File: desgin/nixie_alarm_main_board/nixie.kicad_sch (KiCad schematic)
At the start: 31 parts, among them IC2 HV5530PG-G, IC4 HV5530PG-G, IC6 CD40109BQNSRQ1, Q2 DMN60H080DS-13, Q3 DMN60H080DS-13, Q4 DMN60H080DS-13, Q5 DMN60H080DS-13, Q6 DMN60H080DS-13, Q7 DMN60H080DS-13

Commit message: filter caps
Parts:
- added C6, C7, C8, C9: 100nF 25V, GRM033D70J224ME01D, symbol SamacSys_Parts:GRM033R71E101KA01J
- added R36, R37, R38, R39, R40, R41: 51kΩ, RESC2012X60N, symbol SamacSys_Parts:RK73H2ATTE1003F
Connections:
- net +12V: now also C7.1, C8.1, C9.1
- net GND: now also C6.2, C7.2, C8.2, C9.2, R36.1, R37.1, R38.1, R39.1, R40.1, R41.1; no longer Q2.2 (S), Q3.2 (S), Q4.2 (S), Q5.2 (S), Q6.2 (S), Q7.2 (S)
- net +5V renamed +3.3V
- net +3.3V: now also C6.1
- new net: Q6.2 (S), R40.2
- new net: Q4.2 (S), R38.2
- new net: Q5.2 (S), R39.2
- new net: Q7.2 (S), R41.2
- new net: Q3.2 (S), R37.2
- new net: Q2.2 (S), R36.2
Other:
- moved on the sheet: IC6

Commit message: new rezistors
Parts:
- C6, C7, C8, C9: footprint GRM033D70J224ME01D -> Capacitor_SMD:C_0805_2012Metric_Pad1.18x1.45mm_HandSolder
- R21, R27: value 402kΩ 1/4W -> 390kΩ 1/2W; footprint RESC2012X60N -> Resistor_SMD:R_0805_2012Metric_Pad1.20x1.40mm_HandSolder
- R22, R23, R25, R28, R31, R33: value 25kΩ -> 27kΩ; footprint RESC2012X60N -> Resistor_SMD:R_0805_2012Metric_Pad1.20x1.40mm_HandSolder
- R36, R37, R38, R39, R40, R41: footprint RESC2012X60N -> Resistor_SMD:R_0805_2012Metric_Pad1.20x1.40mm_HandSolder
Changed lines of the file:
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@@
 			)
 		)
-		(property "Footprint" "GRM033D70J224ME01D"
+		(property "Footprint" "Capacitor_SMD:C_0805_2012Metric_Pad1.18x1.45mm_HandSolder"
 			(at -66.218 115.824 0)
 			(effects
@@
 			)
 		)
-		(property "Footprint" "RESC2012X60N"
+		(property "Footprint" "Resistor_SMD:R_0805_2012Metric_Pad1.20x1.40mm_HandSolder"
 			(at 137.49 40.894 0)
 			(effects
@@
 			)
 		)
-		(property "Value" "25kΩ"
+		(property "Value" "27kΩ"
 			(at 254.508 54.864 90)
 			(effects
@@
 			)
 		)
-		(property "Footprint" "RESC2012X60N"
+		(property "Footprint" "Resistor_SMD:R_0805_2012Metric_Pad1.20x1.40mm_HandSolder"
 			(at 165.938 58.674 0)
 			(effects
@@
 			)
 		)
-		(property "Value" "25kΩ"
+		(property "Value" "27kΩ"
 			(at 67.564 53.848 90)
 			(effects
@@
 			)
 		)
-		(property "Footprint" "RESC2012X60N"
+		(property "Footprint" "Resistor_SMD:R_0805_2012Metric_Pad1.20x1.40mm_HandSolder"
 			(at -21.006 57.658 0)
 			(effects
@@
 			)
 		)
-		(property "Footprint" "RESC2012X60N"
+		(property "Footprint" "Resistor_SMD:R_0805_2012Metric_Pad1.20x1.40mm_HandSolder"
 			(at 176.098 40.64 0)
 			(effects
@@
 			)
 		)
-		(property "Footprint" "GRM033D70J224ME01D"
+		(property "Footprint" "Capacitor_SMD:C_0805_2012Metric_Pad1.18x1.45mm_HandSolder"
 			(at -28.372 115.824 0)
 			(effects
@@
 			)
 		)
-		(property "Value" "402kΩ 1/4W"
+		(property "Value" "390kΩ 1/2W"
 			(at 103.378 55.1179 90)
 			(effects
@@
 			)
 		)
-		(property "Footprint" "RESC2012X60N"
+		(property "Footprint" "Resistor_SMD:R_0805_2012Metric_Pad1.20x1.40mm_HandSolder"
 			(at 4.902 58.928 0)
 			(effects
@@
 			)
 		)
-		(property "Footprint" "RESC2012X60N"
+		(property "Footprint" "Resistor_SMD:R_0805_2012Metric_Pad1.20x1.40mm_HandSolder"
 			(at -10.846 39.624 0)
 			(effects
@@
 			)
 		)
-		(property "Value" "25kΩ"
+		(property "Value" "27kΩ"
 			(at 122.174 54.61 90)
 			(effects
@@
 			)
 		)
-		(property "Footprint" "RESC2012X60N"
+		(property "Footprint" "Resistor_SMD:R_0805_2012Metric_Pad1.20x1.40mm_HandSolder"
 			(at 33.35 58.674 0)
 			(effects
@@
 			)
 		)
-		(property "Footprint" "RESC2012X60N"
+		(property "Footprint" "Resistor_SMD:R_0805_2012Metric_Pad1.20x1.40mm_HandSolder"
 			(at 43.51 40.64 0)
 			(effects
@@
 			)
 		)
-		(property "Footprint" "GRM033D70J224ME01D"
+		(property "Footprint" "Capacitor_SMD:C_0805_2012Metric_Pad1.18x1.45mm_HandSolder"
 			(at -65.71 141.732 0)
 			(effects
@@
 			)
 		)
-		(property "Footprint" "RESC2012X60N"
+		(property "Footprint" "Resistor_SMD:R_0805_2012Metric_Pad1.20x1.40mm_HandSolder"
 			(at -50.216 40.132 0)
 			(effects
@@
 			)
 		)
-		(property "Footprint" "RESC2012X60N"
+		(property "Footprint" "Resistor_SMD:R_0805_2012Metric_Pad1.20x1.40mm_HandSolder"
 			(at 82.372 40.132 0)
 			(effects
@@
 			)
 		)
-		(property "Value" "25kΩ"
+		(property "Value" "27kΩ"
 			(at 161.036 55.118 90)
 			(effects
@@
 			)
 		)
-		(property "Footprint" "RESC2012X60N"
+		(property "Footprint" "Resistor_SMD:R_0805_2012Metric_Pad1.20x1.40mm_HandSolder"
 			(at 72.212 58.42 0)
 			(effects
@@
 			)
 		)
-		(property "Value" "25kΩ"
+		(property "Value" "27kΩ"
 			(at 215.9 55.118 90)
 			(effects
@@
 			)
 		)
-		(property "Footprint" "RESC2012X60N"
+		(property "Footprint" "Resistor_SMD:R_0805_2012Metric_Pad1.20x1.40mm_HandSolder"
 			(at 127.33 58.928 0)
 			(effects
@@
 			)
 		)
-		(property "Value" "402kΩ 1/4W"
+		(property "Value" "390kΩ 1/2W"
 			(at 196.342 54.1019 90)
 			(effects
@@
 			)
 		)
-		(property "Footprint" "RESC2012X60N"
+		(property "Footprint" "Resistor_SMD:R_0805_2012Metric_Pad1.20x1.40mm_HandSolder"
 			(at 97.866 57.912 0)
 			(effects
@@
 			)
 		)
-		(property "Footprint" "GRM033D70J224ME01D"
+		(property "Footprint" "Capacitor_SMD:C_0805_2012Metric_Pad1.18x1.45mm_HandSolder"
 			(at -27.864 141.732 0)
 			(effects
@@
 			)
 		)
-		(property "Value" "25kΩ"
+		(property "Value" "27kΩ"
 			(at 28.448 54.356 90)
 			(effects
@@
 			)
 		)
-		(property "Footprint" "RESC2012X60N"
+		(property "Footprint" "Resistor_SMD:R_0805_2012Metric_Pad1.20x1.40mm_HandSolder"
 			(at -60.376 58.166 0)
 			(effects

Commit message: new caps footprint
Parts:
- R24, R26, R29, R30, R32, R34: footprint ERJUP6 -> Resistor_SMD:R_0805_2012Metric_Pad1.20x1.40mm_HandSolder
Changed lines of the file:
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@@
 			)
 		)
-		(property "Footprint" "ERJUP6"
+		(property "Footprint" "Resistor_SMD:R_0805_2012Metric_Pad1.20x1.40mm_HandSolder"
 			(at 282.372 35.052 0)
 			(effects
@@
 			)
 		)
-		(property "Footprint" "ERJUP6"
+		(property "Footprint" "Resistor_SMD:R_0805_2012Metric_Pad1.20x1.40mm_HandSolder"
 			(at 189.154 34.544 0)
 			(effects
@@
 			)
 		)
-		(property "Footprint" "ERJUP6"
+		(property "Footprint" "Resistor_SMD:R_0805_2012Metric_Pad1.20x1.40mm_HandSolder"
 			(at 149.784 35.052 0)
 			(effects
@@
 			)
 		)
-		(property "Footprint" "ERJUP6"
+		(property "Footprint" "Resistor_SMD:R_0805_2012Metric_Pad1.20x1.40mm_HandSolder"
 			(at 243.51 35.56 0)
 			(effects
@@
 			)
 		)
-		(property "Footprint" "ERJUP6"
+		(property "Footprint" "Resistor_SMD:R_0805_2012Metric_Pad1.20x1.40mm_HandSolder"
 			(at 337.49 35.814 0)
 			(effects
@@
 			)
 		)
-		(property "Footprint" "ERJUP6"
+		(property "Footprint" "Resistor_SMD:R_0805_2012Metric_Pad1.20x1.40mm_HandSolder"
 			(at 376.098 35.56 0)
 			(effects

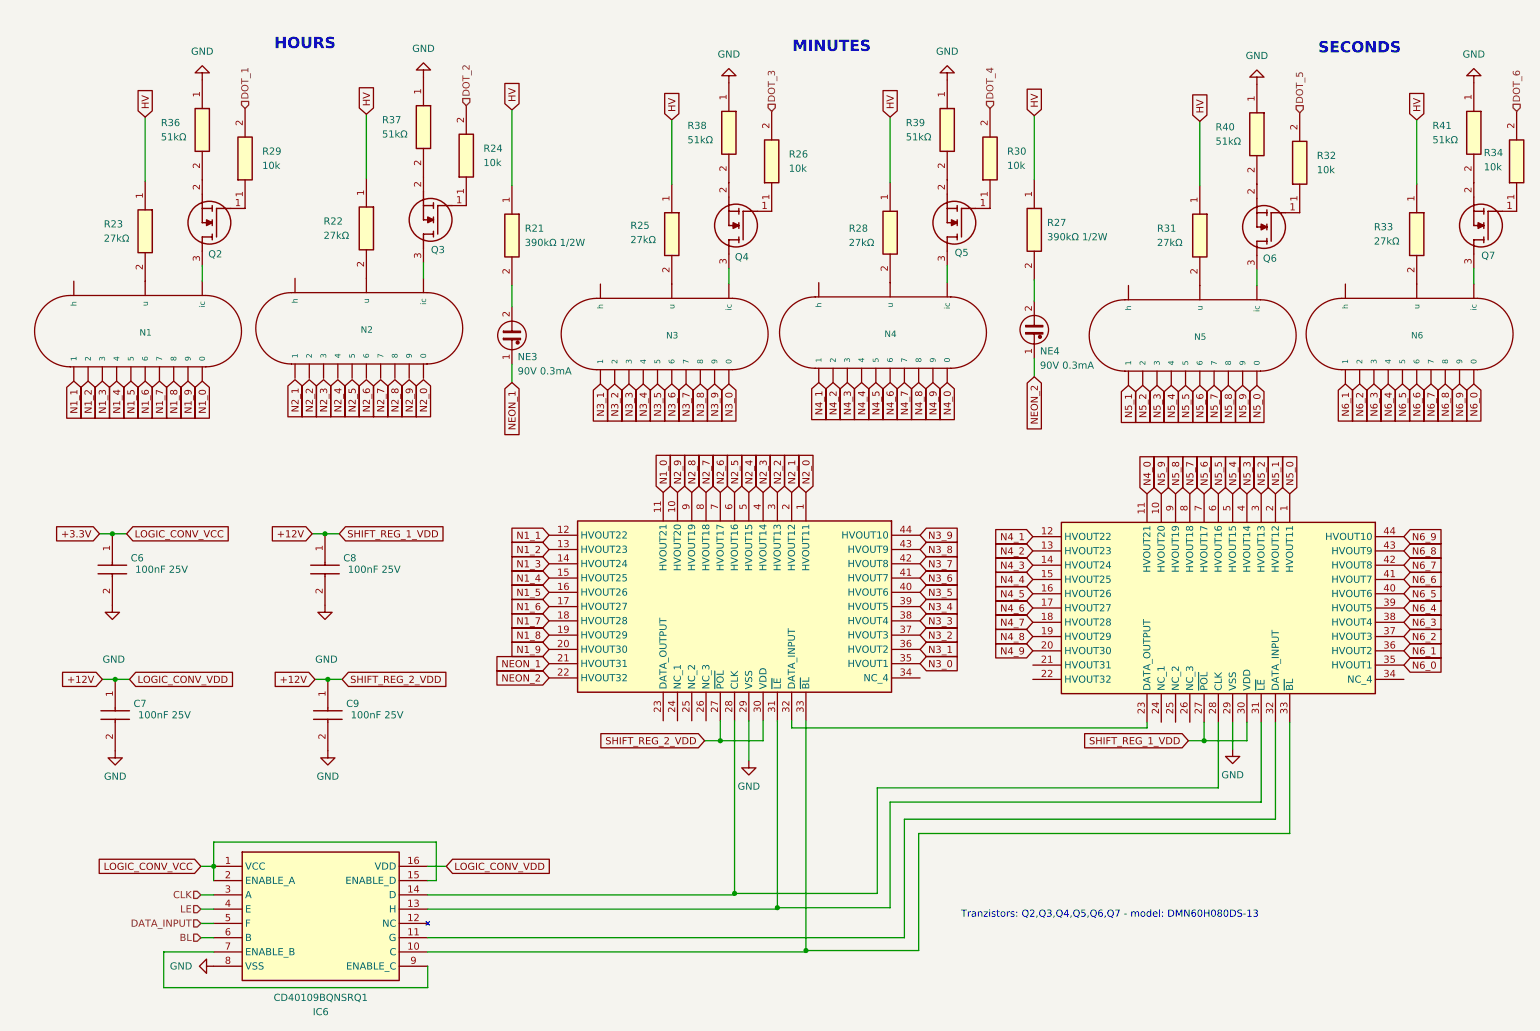
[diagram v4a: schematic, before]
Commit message: traces for nixie tubes
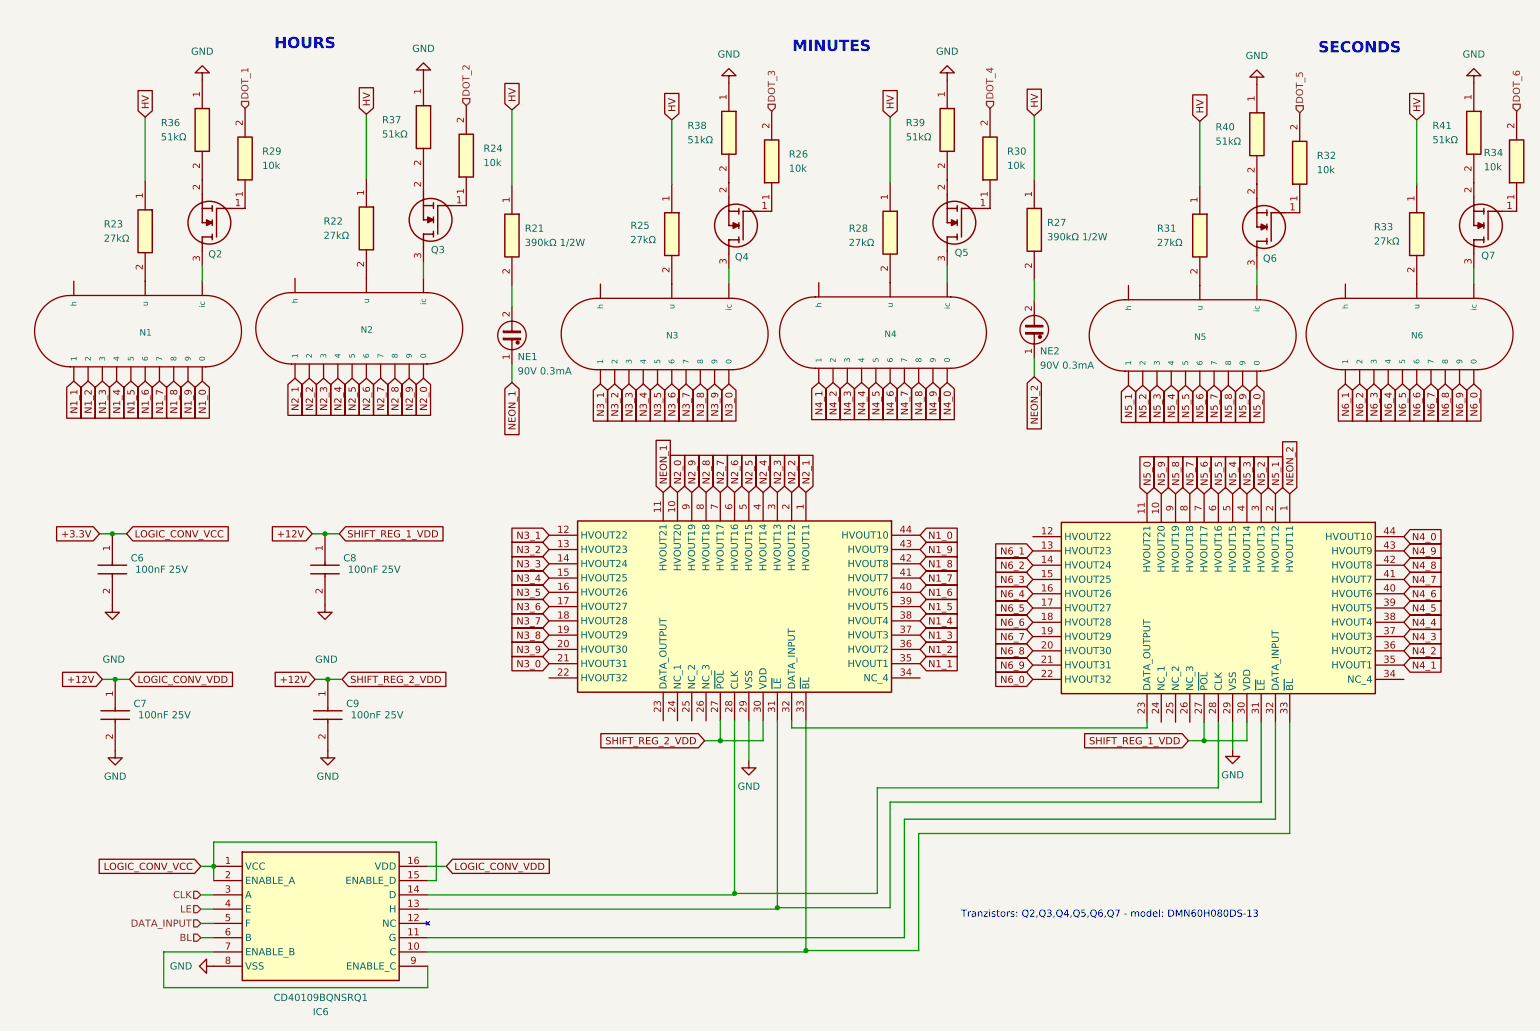
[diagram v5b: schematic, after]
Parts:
- renumbered NE3 to NE1, NE4 to NE2
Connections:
- net N1_0: now also IC2.44 (HVOUT10); no longer IC2.11 (HVOUT21)
- net N1_1: now also IC2.35 (HVOUT1); no longer IC2.12 (HVOUT22)
- net N1_2: now also IC2.36 (HVOUT2); no longer IC2.13 (HVOUT23)
- net N1_3: now also IC2.37 (HVOUT3); no longer IC2.14 (HVOUT24)
- net N1_4: now also IC2.38 (HVOUT4); no longer IC2.15 (HVOUT25)
- net N1_5: now also IC2.39 (HVOUT5); no longer IC2.16 (HVOUT26)
- net N1_6: now also IC2.40 (HVOUT6); no longer IC2.17 (HVOUT27)
- net N1_7: now also IC2.41 (HVOUT7); no longer IC2.18 (HVOUT28)
- net N1_8: now also IC2.42 (HVOUT8); no longer IC2.19 (HVOUT29)
- net N1_9: now also IC2.43 (HVOUT9); no longer IC2.20 (HVOUT30)
- net N2_0: now also IC2.10 (HVOUT20), N2.0; no longer IC2.1 (HVOUT11)
- net N2_1: now also IC2.1 (HVOUT11), N2.1; no longer IC2.2 (HVOUT12)
- net N2_2: now also IC2.2 (HVOUT12), N2.2; no longer IC2.3 (HVOUT13)
- net N2_3: now also IC2.3 (HVOUT13), N2.3; no longer IC2.4 (HVOUT14)
- net N2_4: now also IC2.4 (HVOUT14), N2.4; no longer IC2.5 (HVOUT15)
- net N2_5: now also IC2.5 (HVOUT15), N2.5; no longer IC2.6 (HVOUT16)
- net N2_6: now also IC2.6 (HVOUT16), N2.6; no longer IC2.7 (HVOUT17)
- net N2_7: now also IC2.7 (HVOUT17), N2.7; no longer IC2.8 (HVOUT18)
- net N2_8: now also IC2.8 (HVOUT18), N2.8; no longer IC2.9 (HVOUT19)
- net N2_9: now also IC2.9 (HVOUT19), N2.9; no longer IC2.10 (HVOUT20)
- net N3_0: now also IC2.21 (HVOUT31); no longer IC2.35 (HVOUT1)
- net N3_1: now also IC2.12 (HVOUT22); no longer IC2.36 (HVOUT2)
- net N3_2: now also IC2.13 (HVOUT23); no longer IC2.37 (HVOUT3)
- net N3_3: now also IC2.14 (HVOUT24); no longer IC2.38 (HVOUT4)
- net N3_4: now also IC2.15 (HVOUT25); no longer IC2.39 (HVOUT5)
- net N3_5: now also IC2.16 (HVOUT26); no longer IC2.40 (HVOUT6)
- net N3_6: now also IC2.17 (HVOUT27); no longer IC2.41 (HVOUT7)
- net N3_7: now also IC2.18 (HVOUT28); no longer IC2.42 (HVOUT8)
- net N3_8: now also IC2.19 (HVOUT29); no longer IC2.43 (HVOUT9)
- net N3_9: now also IC2.20 (HVOUT30); no longer IC2.44 (HVOUT10)
- net N4_0: now also IC4.44 (HVOUT10); no longer IC4.11 (HVOUT21)
- net N4_1: now also IC4.35 (HVOUT1); no longer IC4.12 (HVOUT22)
- net N4_2: now also IC4.36 (HVOUT2); no longer IC4.13 (HVOUT23)
- net N4_3: now also IC4.37 (HVOUT3); no longer IC4.14 (HVOUT24)
- net N4_4: now also IC4.38 (HVOUT4); no longer IC4.15 (HVOUT25)
- net N4_5: now also IC4.39 (HVOUT5); no longer IC4.16 (HVOUT26)
- net N4_6: now also IC4.40 (HVOUT6); no longer IC4.17 (HVOUT27)
- net N4_7: now also IC4.41 (HVOUT7); no longer IC4.18 (HVOUT28)
- net N4_8: now also IC4.42 (HVOUT8); no longer IC4.19 (HVOUT29)
- net N4_9: now also IC4.43 (HVOUT9); no longer IC4.20 (HVOUT30)
- net N5_0: now also IC4.11 (HVOUT21); no longer IC4.1 (HVOUT11)
- net N6_0: now also IC4.22 (HVOUT32); no longer IC4.35 (HVOUT1)
- net N6_1: now also IC4.13 (HVOUT23); no longer IC4.36 (HVOUT2)
- net N6_2: now also IC4.14 (HVOUT24); no longer IC4.37 (HVOUT3)
- net N6_3: now also IC4.15 (HVOUT25); no longer IC4.38 (HVOUT4)
- net N6_4: now also IC4.16 (HVOUT26); no longer IC4.39 (HVOUT5)
- net N6_5: now also IC4.17 (HVOUT27); no longer IC4.40 (HVOUT6)
- net N6_6: now also IC4.18 (HVOUT28); no longer IC4.41 (HVOUT7)
- net N6_7: now also IC4.19 (HVOUT29); no longer IC4.42 (HVOUT8)
- net N6_8: now also IC4.20 (HVOUT30); no longer IC4.43 (HVOUT9)
- net N6_9: now also IC4.21 (HVOUT31); no longer IC4.44 (HVOUT10)
- net NEON_1: now also IC2.11 (HVOUT21); no longer IC2.21 (HVOUT31)
- net NEON_2: now also IC4.1 (HVOUT11); no longer IC2.22 (HVOUT32)

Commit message: board v1
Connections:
- net +3.3V: now also IC6.7 (ENABLE_B), IC6.9 (ENABLE_C)
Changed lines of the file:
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@@
 	)
 	(junction
+		(at 87.63 183.896)
+		(diameter 0)
+		(color 0 0 0 0)
+	)
+	(junction
 		(at 224.282 143.764)
 		(diameter 0)
@@
 	)
 	(junction
+		(at 87.63 168.656)
+		(diameter 0)
+		(color 0 0 0 0)
+	)
+	(junction
 		(at 67.818 106.934)
 		(diameter 0)
@@
 	(wire
 		(pts
+			(xy 87.63 168.656) (xy 87.63 183.896)
+		)
+		(stroke
+			(width 0)
+			(type default)
+		)
+	)
+	(wire
+		(pts
 			(xy 194.056 65.532) (xy 194.056 61.722)
 		)
@@
 	(wire
 		(pts
-			(xy 45.72 166.116) (xy 48.006 166.116)
+			(xy 42.418 166.116) (xy 48.006 166.116)
 		)
 		(stroke
@@
 	(wire
 		(pts
-			(xy 39.116 187.706) (xy 86.106 187.706)
+			(xy 39.116 187.706) (xy 87.63 187.706)
 		)
 		(stroke
@@
 	(wire
 		(pts
+			(xy 86.106 183.896) (xy 87.63 183.896)
+		)
+		(stroke
+			(width 0)
+			(type default)
+		)
+	)
+	(wire
+		(pts
 			(xy 101.092 66.548) (xy 101.092 62.738)
 		)
@@
 	(wire
 		(pts
-			(xy 86.106 187.706) (xy 86.106 183.896)
+			(xy 87.63 187.706) (xy 87.63 183.896)
 		)
 		(stroke
@@
 	(global_label "LOGIC_CONV_VCC"
 		(shape input)
-		(at 45.72 166.116 180)
+		(at 42.418 166.116 180)
 		(fields_autoplaced yes)
 		(effects
@@
 		)
 		(property "Intersheetrefs" "${INTERSHEET_REFS}"
-			(at 26.648 166.116 0)
+			(at 23.346 166.116 0)
 			(effects
 				(font

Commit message: fixes added
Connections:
- net GND: now also Q2.2 (S), Q3.2 (S), Q4.2 (S), Q5.2 (S), Q6.2 (S), Q7.2 (S); no longer R36.1, R37.1, R38.1, R39.1, R40.1, R41.1
- net at R40.2: now also N5.ic; no longer Q6.2 (S)
- net at Q6.3 (D): now also R40.1; no longer N5.ic
- net at R38.2: now also N3.ic; no longer Q4.2 (S)
- net at Q4.3 (D): now also R38.1; no longer N3.ic
- net at R39.2: now also N4.ic; no longer Q5.2 (S)
- net at Q5.3 (D): now also R39.1; no longer N4.ic
- net at N1.ic: now also R36.2; no longer Q2.3 (D)
- net at R41.2: now also N6.ic; no longer Q7.2 (S)
- net at Q7.3 (D): now also R41.1; no longer N6.ic
- net at N2.ic: now also R37.2; no longer Q3.3 (D)
- new net: Q3.3 (D), R37.1
- new net: Q2.3 (D), R36.1
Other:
- moved on the sheet: N2, N4, N5, N6, NE1, NE2, Q2, Q4, Q5, Q6, Q7, R21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

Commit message: koncepcja układu
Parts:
- R22, R23, R25, R28, R31, R33: value 27kΩ -> 35.7kΩ
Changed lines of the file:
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@@
 		(dnp no)
 		(property "Reference" "R33"
-			(at 255.27 52.07 90)
+			(at 253.492 52.324 90)
 			(effects
 				(font
@@
 			)
 		)
-		(property "Value" "27kΩ"
-			(at 255.27 54.61 90)
+		(property "Value" "35.7kΩ"
+			(at 253.492 54.864 90)
 			(effects
 				(font
@@
 		(dnp no)
 		(property "Reference" "R22"
-			(at 67.31 52.07 90)
+			(at 65.278 51.816 90)
 			(effects
 				(font
@@
 			)
 		)
-		(property "Value" "27kΩ"
-			(at 67.31 54.61 90)
+		(property "Value" "35.7kΩ"
+			(at 65.278 54.356 90)
 			(effects
 				(font
@@
 		(dnp no)
 		(property "Reference" "R25"
-			(at 122.174 52.07 90)
+			(at 120.142 52.07 90)
 			(effects
 				(font
@@
 			)
 		)
-		(property "Value" "27kΩ"
-			(at 122.174 54.61 90)
+		(property "Value" "35.7kΩ"
+			(at 120.142 54.61 90)
 			(effects
 				(font
@@
 		(dnp no)
 		(property "Reference" "R28"
-			(at 161.544 52.578 90)
+			(at 160.02 52.578 90)
 			(effects
 				(font
@@
 			)
 		)
-		(property "Value" "27kΩ"
-			(at 161.544 55.118 90)
+		(property "Value" "35.7kΩ"
+			(at 160.02 55.118 90)
 			(effects
 				(font
@@
 		(dnp no)
 		(property "Reference" "R31"
-			(at 215.9 52.578 90)
+			(at 214.122 52.832 90)
 			(effects
 				(font
@@
 			)
 		)
-		(property "Value" "27kΩ"
-			(at 215.9 55.118 90)
+		(property "Value" "35.7kΩ"
+			(at 214.122 55.372 90)
 			(effects
 				(font
@@
 		(dnp no)
 		(property "Reference" "R23"
-			(at 28.194 49.53 90)
+			(at 25.146 49.53 90)
 			(effects
 				(font
@@
 			)
 		)
-		(property "Value" "27kΩ"
-			(at 28.194 52.07 90)
+		(property "Value" "35.7kΩ"
+			(at 25.146 52.07 90)
 			(effects
 				(font
